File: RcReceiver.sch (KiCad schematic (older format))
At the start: 13 parts, among them U1 STM32L476VGT6, Y1 16MHz

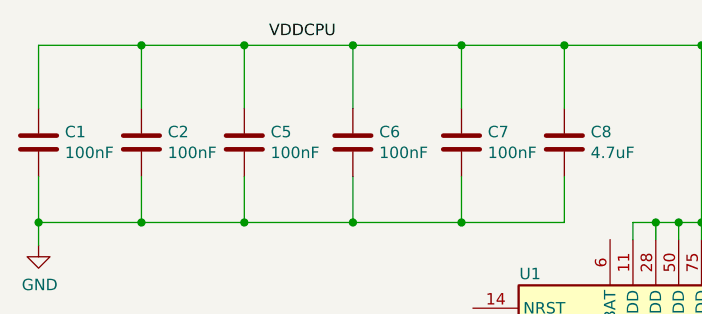
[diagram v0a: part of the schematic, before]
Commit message: Add footprints
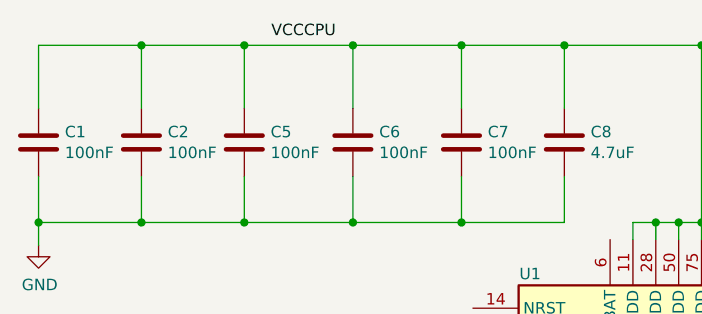
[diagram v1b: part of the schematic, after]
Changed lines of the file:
@@
 $EndComp
 Text Label 2025 900  2    50   ~ 0
-VDDCPU
+VCCCPU
 $Comp
 L Device:C C8

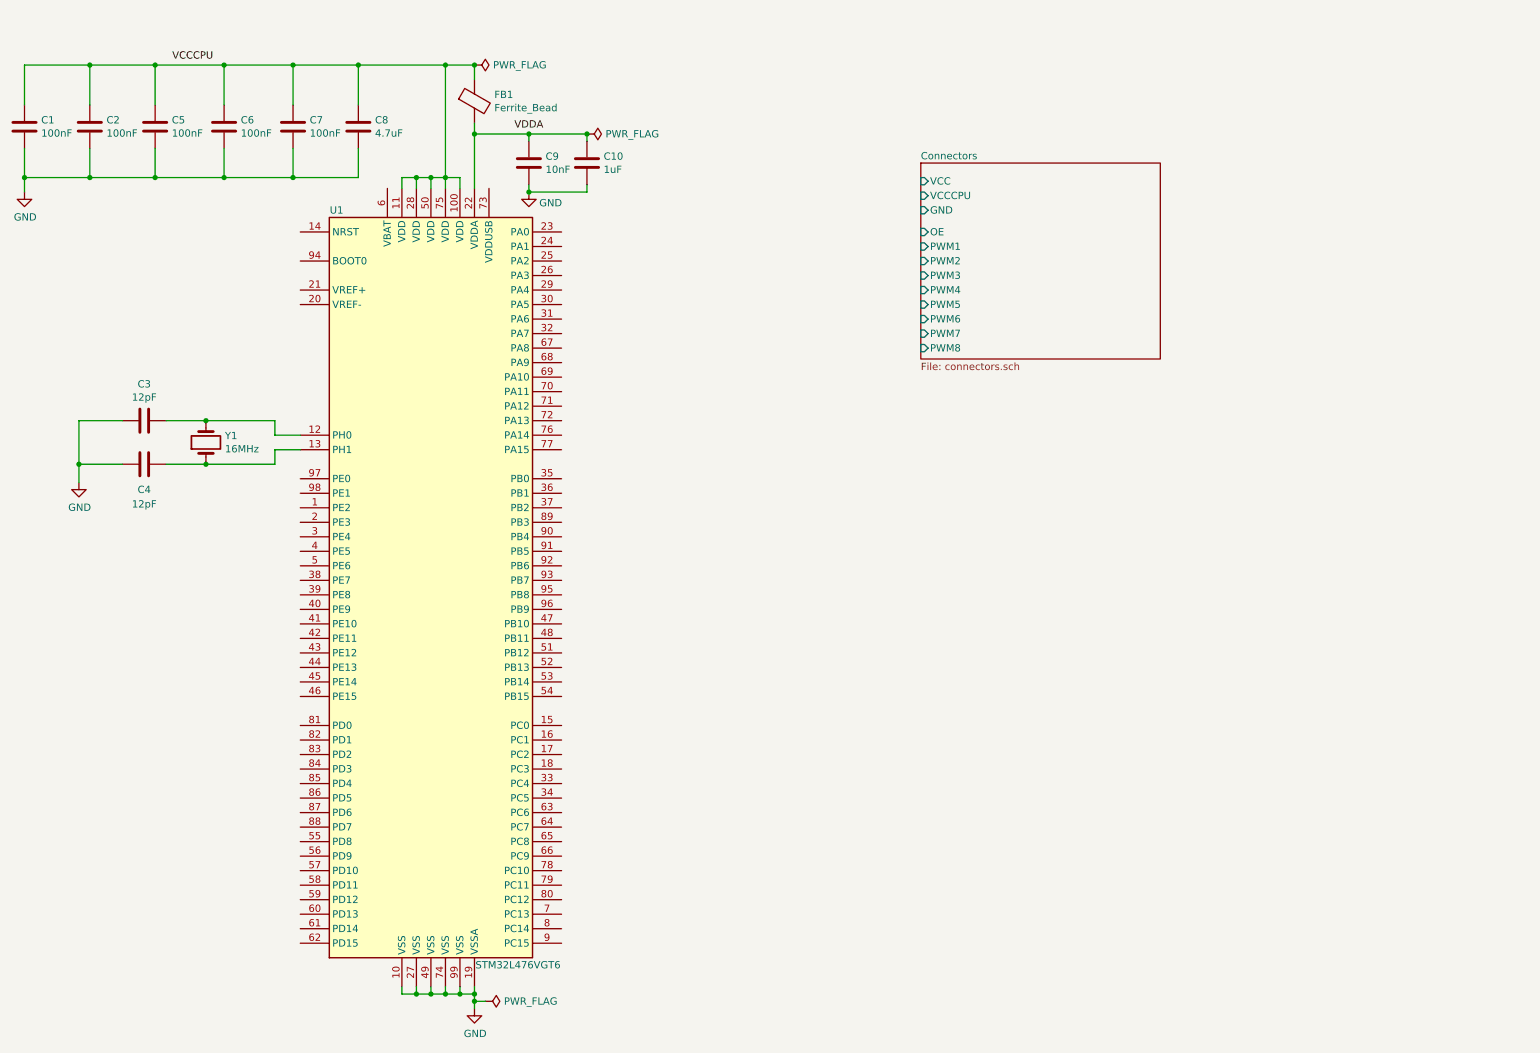
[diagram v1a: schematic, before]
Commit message: Add schema with RF modules
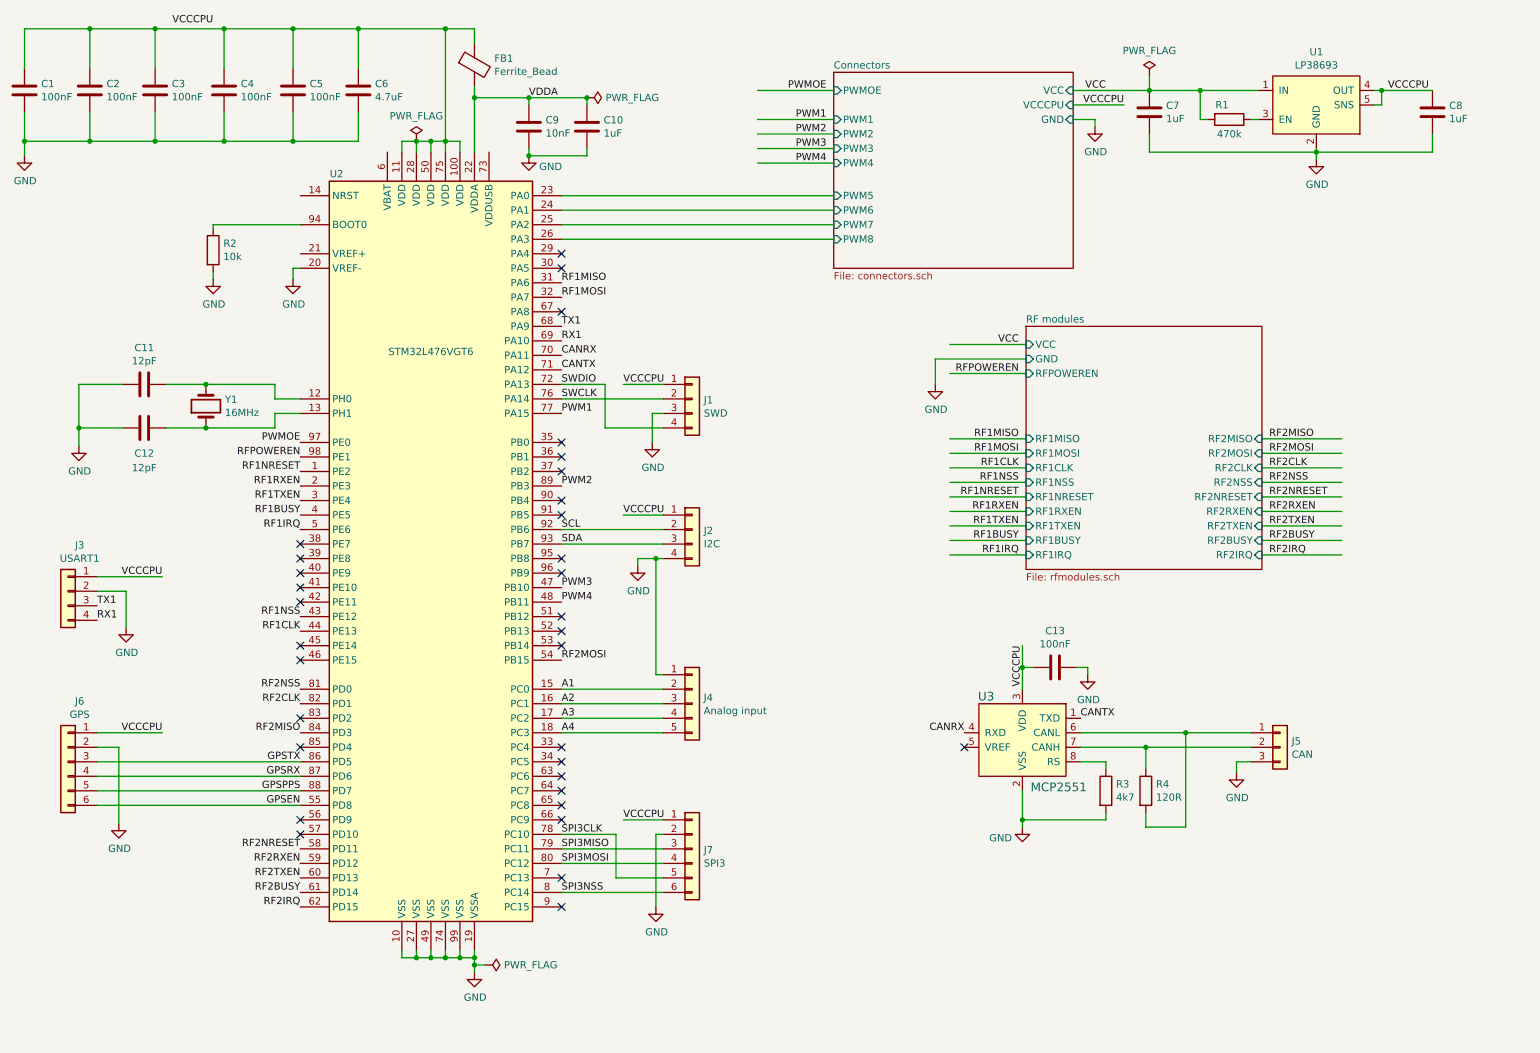
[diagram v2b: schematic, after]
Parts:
- added C13: 100nF, symbol Device:C
- added C7, C8: 1uF, symbol Device:C
- added J1: SWD, symbol Connector_Generic:Conn_01x04
- added J2: I2C, symbol Connector_Generic:Conn_01x04
- added J3: USART1, symbol Connector_Generic:Conn_01x04
- added J4: Analog input, symbol Connector_Generic:Conn_01x05
- added J5: CAN, symbol Connector_Generic:Conn_01x03
- added J6: GPS, symbol Connector_Generic:Conn_01x06
- added J7: SPI3, symbol Connector_Generic:Conn_01x06
- added R1: 470k, symbol Device:R
- added R2: 10k, symbol Device:R
- added R3: 4k7, symbol Device:R
- added R4: 120R, symbol Device:R
- added U1: LP38693, symbol LP38693:LP38693
- added U3: MCP2551, digikey-footprints:SOIC-8_W3.9mm, symbol dk_Interface-Drivers-Receivers-Transceivers:MCP2551-I_SN
- renumbered C3 to C11, C4 to C12, C5 to C3, C6 to C4, C7 to C5, C8 to C6, U1 to U2
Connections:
- net labels added: A1, A2, A3, A4, CANRX, CANTX, GPSEN, GPSPPS, GPSRX, GPSTX, PWM1, PWM2, PWM3, PWM4, PWMOE, RF1BUSY, RF1CLK, RF1IRQ, RF1MISO, RF1MOSI, RF1NRESET, RF1NSS, RF1RXEN, RF1TXEN, RF2BUSY, RF2CLK, RF2IRQ, RF2MISO, RF2MOSI, RF2NRESET, RF2NSS, RF2RXEN, RF2TXEN, RFPOWEREN, RX1, SCL, SDA, SPI3CLK, SPI3MISO, SPI3MOSI, SPI3NSS, SWCLK, SWDIO, TX1, VCC
- wire segments 71 -> 186
- no-connect marks 0 -> 33
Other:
- moved on the sheet: C1, C10, C11, C12, C2, C3, C4, C5, C6, C9, FB1, U2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

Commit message: Small changes
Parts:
- removed C13: 100nF, symbol Device:C
- removed J1: SWD, symbol Connector_Generic:Conn_01x04
- removed J5: CAN, symbol Connector_Generic:Conn_01x03
- removed R3: 4k7, symbol Device:R
- removed U3: MCP2551, digikey-footprints:SOIC-8_W3.9mm, symbol dk_Interface-Drivers-Receivers-Transceivers:MCP2551-I_SN
- added C11: 1uF, symbol Device:C
- added C12: 100nF, symbol Device:C
- added D1: LED, symbol Device:LED
- added D2: LED_ARGB, symbol Device:LED_ARGB
- added J1: VBAT, symbol Connector_Generic:Conn_01x02
- added J2: SWD, symbol Connector_Generic:Conn_01x05
- added R1: 2k2, symbol Device:R
- added R5, R6: 1k, symbol Device:R
- R4: value 120R -> 1k
- U1: value LP38693 -> LP38693-3.3
- renumbered C11 to C13, C12 to C14, J2 to J3, J3 to J4, J4 to J5, R1 to R2, R2 to R3
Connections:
- net labels added: LEDBLUE, LEDGREEN, LEDRED, NRST, VBAT
- wire segments 186 -> 190
- no-connect marks 33 -> 30
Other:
- moved on the sheet: J3, R3

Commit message: Final changes in schema
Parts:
- removed C11: 1uF, symbol Device:C
- removed C12: 100nF, symbol Device:C
- removed J3: I2C, symbol Connector_Generic:Conn_01x04
- removed J7: SPI3, symbol Connector_Generic:Conn_01x06
- added J3: I2C, symbol Connector_Generic:Conn_01x05
- added J7: SPI3, symbol Connector_Generic:Conn_01x07
- renumbered C13 to C11, C14 to C12
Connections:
- wire segments 190 -> 182
- no-connect marks 30 -> 29
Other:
- moved on the sheet: R3

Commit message: Add some footprints
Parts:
- removed Y1: 16MHz, symbol Device:Crystal
- added Y1: 16MHz, Oscillator:Oscillator_SMD_SeikoEpson_SG210-4Pin_2.5x2.0mm, symbol Device:Crystal_GND24
- C1, C10, C11, C12, C2, C3, C4, C5, C6, C7, C8, C9: footprint (none) -> Capacitor_SMD:C_0402_1005Metric
- D1: footprint (none) -> LED_SMD:LED_0402_1005Metric
- FB1: footprint (none) -> Inductor_SMD:L_0402_1005Metric
- J1: footprint (none) -> Connector_PinHeader_1.27mm:PinHeader_1x02_P1.27mm_Vertical
- J2, J3, J5: footprint (none) -> Connector_JST:JST_SH_BM05B-SRSS-TB_1x05-1MP_P1.00mm_Vertical
- J4: footprint (none) -> Connector_JST:JST_SH_BM04B-SRSS-TB_1x04-1MP_P1.00mm_Vertical
- J6: footprint (none) -> Connector_JST:JST_SH_BM06B-SRSS-TB_1x06-1MP_P1.00mm_Vertical
- J7: footprint (none) -> Connector_JST:JST_SH_BM07B-SRSS-TB_1x07-1MP_P1.00mm_Vertical
- R1, R2, R3, R4: footprint (none) -> Resistor_SMD:R_0402_1005Metric
- R5, R6: value 1k -> 470; footprint (none) -> Resistor_SMD:R_0402_1005Metric
- U1: footprint (none) -> miscellaneous:WSON-6_3x3mm_Pitch0.95mm
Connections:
- wire segments 182 -> 188
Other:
- moved on the sheet: C11, C12
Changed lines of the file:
@@
 EESchema Schematic File Version 4
+LIBS:RcReceiver-cache
 EELAYER 26 0
 EELAYER END
@@
 $EndDescr
 $Comp
-L Device:Crystal Y1
-U 1 1 5C749939
-P 1975 3275
-F 0 "Y1" V 2021 3144 50  0000 R CNN
-F 1 "16MHz" V 1930 3144 50  0000 R CNN
-F 2 "" H 1975 3275 50  0001 C CNN
-F 3 "~" H 1975 3275 50  0001 C CNN
-	1    1975 3275
-	0    -1   -1   0
-$EndComp
-$Comp
 L Device:C C12
 U 1 1 5C749996
-P 1550 3425
-F 0 "C12" V 1725 3425 50  0000 C CNN
-F 1 "12pF" V 1825 3425 50  0000 C CNN
-F 2 "" H 1588 3275 50  0001 C CNN
-F 3 "~" H 1550 3425 50  0001 C CNN
-	1    1550 3425
+P 1375 3450
+F 0 "C12" V 1550 3450 50  0000 C CNN
+F 1 "12pF" V 1650 3450 50  0000 C CNN
+F 2 "Capacitor_SMD:C_0402_1005Metric" H 1413 3300 50  0001 C CNN
+F 3 "~" H 1375 3450 50  0001 C CNN
+	1    1375 3450
 	0    1    1    0
 $EndComp
@@
 L Device:C C11
 U 1 1 5C7499E6
-P 1550 3125
-F 0 "C11" V 1298 3125 50  0000 C CNN
-F 1 "12pF" V 1389 3125 50  0000 C CNN
-F 2 "" H 1588 2975 50  0001 C CNN
-F 3 "~" H 1550 3125 50  0001 C CNN
-	1    1550 3125
+P 1375 3100
+F 0 "C11" V 1123 3100 50  0000 C CNN
+F 1 "12pF" V 1214 3100 50  0000 C CNN
+F 2 "Capacitor_SMD:C_0402_1005Metric" H 1413 2950 50  0001 C CNN
+F 3 "~" H 1375 3100 50  0001 C CNN
+	1    1375 3100
 	0    1    1    0
 $EndComp
 Wire Wire Line
-	1700 3425 1975 3425
-Wire Wire Line
-	1975 3425 2450 3425
-Wire Wire Line
-	2450 3425 2450 3325
+	2450 3450 2450 3325
 Wire Wire Line
 	2450 3325 2625 3325
-Connection ~ 1975 3425
-Wire Wire Line
-	1700 3125 1975 3125
-Wire Wire Line
-	1975 3125 2450 3125
-Wire Wire Line
-	2450 3125 2450 3225
 Wire Wire Line
 	2450 3225 2625 3225
-Connection ~ 1975 3125
 $Comp
 L power:GND #PWR010
@@
 $EndComp
 Wire Wire Line
-	1100 3550 1100 3425
-Wire Wire Line
-	1100 3125 1400 3125
-Wire Wire Line
-	1400 3425 1100 3425
-Connection ~ 1100 3425
-Wire Wire Line
-	1100 3425 1100 3125
+	1100 3550 1100 3450
+Wire Wire Line
+	1100 3100 1225 3100
+Wire Wire Line
+	1225 3450 1100 3450
+Connection ~ 1100 3450
+Wire Wire Line
+	1100 3450 1100 3100
 $Comp
 L power:PWR_FLAG #FLG04
@@
 F 0 "C1" H 840 1146 50  0000 L CNN
 F 1 "100nF" H 840 1055 50  0000 L CNN
-F 2 "" H 763 950 50  0001 C CNN
+F 2 "Capacitor_SMD:C_0402_1005Metric" H 763 950 50  0001 C CNN
 F 3 "~" H 725 1100 50  0001 C CNN
 	1    725  1100
@@
 F 0 "C2" H 1290 1146 50  0000 L CNN
 F 1 "100nF" H 1290 1055 50  0000 L CNN
-F 2 "" H 1213 950 50  0001 C CNN
+F 2 "Capacitor_SMD:C_0402_1005Metric" H 1213 950 50  0001 C CNN
 F 3 "~" H 1175 1100 50  0001 C CNN
 	1    1175 1100
@@
 F 0 "C3" H 1740 1146 50  0000 L CNN
 F 1 "100nF" H 1740 1055 50  0000 L CNN
-F 2 "" H 1663 950 50  0001 C CNN
+F 2 "Capacitor_SMD:C_0402_1005Metric" H 1663 950 50  0001 C CNN
 F 3 "~" H 1625 1100 50  0001 C CNN
 	1    1625 1100
@@
 F 0 "C4" H 2215 1146 50  0000 L CNN
 F 1 "100nF" H 2215 1055 50  0000 L CNN
-F 2 "" H 2138 950 50  0001 C CNN
+F 2 "Capacitor_SMD:C_0402_1005Metric" H 2138 950 50  0001 C CNN
 F 3 "~" H 2100 1100 50  0001 C CNN
 	1    2100 1100
@@
 F 0 "C5" H 2690 1146 50  0000 L CNN
 F 1 "100nF" H 2690 1055 50  0000 L CNN
-F 2 "" H 2613 950 50  0001 C CNN
+F 2 "Capacitor_SMD:C_0402_1005Metric" H 2613 950 50  0001 C CNN
 F 3 "~" H 2575 1100 50  0001 C CNN
 	1    2575 1100
@@
 F 0 "C6" H 3140 1146 50  0000 L CNN
 F 1 "4.7uF" H 3140 1055 50  0000 L CNN
-F 2 "" H 3063 950 50  0001 C CNN
+F 2 "Capacitor_SMD:C_0402_1005Metric" H 3063 950 50  0001 C CNN
 F 3 "~" H 3025 1100 50  0001 C CNN
 	1    3025 1100
@@
 F 0 "C9" H 4315 1396 50  0000 L CNN
 F 1 "10nF" H 4315 1305 50  0000 L CNN
-F 2 "" H 4238 1200 50  0001 C CNN
+F 2 "Capacitor_SMD:C_0402_1005Metric" H 4238 1200 50  0001 C CNN
 F 3 "~" H 4200 1350 50  0001 C CNN
 	1    4200 1350
@@
 F 0 "C10" H 4715 1396 50  0000 L CNN
 F 1 "1uF" H 4715 1305 50  0000 L CNN
-F 2 "" H 4638 1200 50  0001 C CNN
+F 2 "Capacitor_SMD:C_0402_1005Metric" H 4638 1200 50  0001 C CNN
 F 3 "~" H 4600 1350 50  0001 C CNN
 	1    4600 1350
@@
 F 0 "FB1" H 3962 971 50  0000 L CNN
 F 1 "Ferrite_Bead" H 3962 880 50  0000 L CNN
-F 2 "" V 3755 925 50  0001 C CNN
+F 2 "Inductor_SMD:L_0402_1005Metric" V 3755 925 50  0001 C CNN
 F 3 "~" H 3825 925 50  0001 C CNN
 	1    3825 925
@@
 F 0 "R3" H 2120 2221 50  0000 L CNN
 F 1 "10k" H 2120 2130 50  0000 L CNN
-F 2 "" V 1980 2175 50  0001 C CNN
+F 2 "Resistor_SMD:R_0402_1005Metric" V 1980 2175 50  0001 C CNN
 F 3 "~" H 2050 2175 50  0001 C CNN
 	1    2050 2175
@@
 F 0 "U1" H 9625 1565 50  0000 C CNN
 F 1 "LP38693-3.3" H 9625 1474 50  0000 C CNN
-F 2 "" H 9625 1200 50  0001 C CNN
+F 2 "miscellaneous:WSON-6_3x3mm_Pitch0.95mm" H 9625 1200 50  0001 C CNN
 F 3 "http://www.ti.com/lit/ds/snvs321o/snvs321o.pdf" H 9625 1200 50  0001 C CNN
 	1    9625 1200
@@
 F 0 "C8" H 10540 1296 50  0000 L CNN
 F 1 "1uF" H 10540 1205 50  0000 L CNN
-F 2 "" H 10463 1100 50  0001 C CNN
+F 2 "Capacitor_SMD:C_0402_1005Metric" H 10463 1100 50  0001 C CNN
 F 3 "~" H 10425 1250 50  0001 C CNN
 	1    10425 1250
@@
 F 0 "C7" H 8590 1296 50  0000 L CNN
 F 1 "1uF" H 8590 1205 50  0000 L CNN
-F 2 "" H 8513 1100 50  0001 C CNN
+F 2 "Capacitor_SMD:C_0402_1005Metric" H 8513 1100 50  0001 C CNN
 F 3 "~" H 8475 1250 50  0001 C CNN
 	1    8475 1250
@@
 F 0 "R2" V 8925 1250 50  0000 C CNN
 F 1 "470k" V 9125 1300 50  0000 C CNN
-F 2 "" V 8955 1300 50  0001 C CNN
+F 2 "Resistor_SMD:R_0402_1005Metric" V 8955 1300 50  0001 C CNN
 F 3 "~" H 9025 1300 50  0001 C CNN
 	1    9025 1300
@@
 F 0 "J5" H 5404 5367 50  0000 L CNN
 F 1 "Analog input" H 5404 5276 50  0000 L CNN
-F 2 "" H 5325 5325 50  0001 C CNN
+F 2 "Connector_JST:JST_SH_BM05B-SRSS-TB_1x05-1MP_P1.00mm_Vertical" H 5325 5325 50  0001 C CNN
 F 3 "~" H 5325 5325 50  0001 C CNN
 	1    5325 5325
@@
 F 0 "J6" H 945 6142 50  0000 C CNN
 F 1 "GPS" H 945 6051 50  0000 C CNN
-F 2 "" H 1025 5725 50  0001 C CNN
+F 2 "Connector_JST:JST_SH_BM06B-SRSS-TB_1x06-1MP_P1.00mm_Vertical" H 1025 5725 50  0001 C CNN
 F 3 "~" H 1025 5725 50  0001 C CNN
 	1    1025 5725
@@
 F 0 "J4" H 945 4867 50  0000 C CNN
 F 1 "USART1" H 945 4776 50  0000 C CNN
-F 2 "" H 1025 4550 50  0001 C CNN
+F 2 "Connector_JST:JST_SH_BM04B-SRSS-TB_1x04-1MP_P1.00mm_Vertical" H 1025 4550 50  0001 C CNN
 F 3 "~" H 1025 4550 50  0001 C CNN
 	1    1025 4550
@@
 F 0 "J2" H 5405 3367 50  0000 L CNN
 F 1 "SWD" H 5405 3276 50  0000 L CNN
-F 2 "" H 5325 3325 50  0001 C CNN
+F 2 "Connector_JST:JST_SH_BM05B-SRSS-TB_1x05-1MP_P1.00mm_Vertical" H 5325 3325 50  0001 C CNN
 F 3 "~" H 5325 3325 50  0001 C CNN
 	1    5325 3325
@@
 F 0 "R1" H 10870 1321 50  0000 L CNN
 F 1 "2k2" H 10870 1230 50  0000 L CNN
-F 2 "" V 10730 1275 50  0001 C CNN
+F 2 "Resistor_SMD:R_0402_1005Metric" V 10730 1275 50  0001 C CNN
 F 3 "~" H 10800 1275 50  0001 C CNN
 	1    10800 1275
@@
 F 0 "D1" V 10838 1633 50  0000 R CNN
 F 1 "LED" V 10747 1633 50  0000 R CNN
-F 2 "" H 10800 1750 50  0001 C CNN
+F 2 "LED_SMD:LED_0402_1005Metric" H 10800 1750 50  0001 C CNN
 F 3 "~" H 10800 1750 50  0001 C CNN
 	1    10800 1750
@@
 F 0 "R4" V 1750 6975 50  0000 C CNN
 F 1 "1k" V 1825 6975 50  0000 C CNN
-F 2 "" V 1755 6975 50  0001 C CNN
+F 2 "Resistor_SMD:R_0402_1005Metric" V 1755 6975 50  0001 C CNN
 F 3 "~" H 1825 6975 50  0001 C CNN
 	1    1825 6975
@@
 P 1825 7175
 F 0 "R5" V 1750 7175 50  0000 C CNN
-F 1 "1k" V 1825 7175 50  0000 C CNN
-F 2 "" V 1755 7175 50  0001 C CNN
+F 1 "470" V 1825 7175 50  0000 C CNN
+F 2 "Resistor_SMD:R_0402_1005Metric" V 1755 7175 50  0001 C CNN
 F 3 "~" H 1825 7175 50  0001 C CNN
 	1    1825 7175
@@
 P 1825 7375
 F 0 "R6" V 1750 7375 50  0000 C CNN
-F 1 "1k" V 1825 7375 50  0000 C CNN
-F 2 "" V 1755 7375 50  0001 C CNN
+F 1 "470" V 1825 7375 50  0000 C CNN
+F 2 "Resistor_SMD:R_0402_1005Metric" V 1755 7375 50  0001 C CNN
 F 3 "~" H 1825 7375 50  0001 C CNN
 	1    1825 7375
@@
 F 0 "J1" H 5404 2442 50  0000 L CNN
 F 1 "VBAT" H 5404 2351 50  0000 L CNN
-F 2 "" H 5325 2450 50  0001 C CNN
+F 2 "Connector_PinHeader_1.27mm:PinHeader_1x02_P1.27mm_Vertical" H 5325 2450 50  0001 C CNN
 F 3 "~" H 5325 2450 50  0001 C CNN
 	1    5325 2450
@@
 F 0 "J3" H 5405 4167 50  0000 L CNN
 F 1 "I2C" H 5405 4076 50  0000 L CNN
-F 2 "" H 5325 4125 50  0001 C CNN
+F 2 "Connector_JST:JST_SH_BM05B-SRSS-TB_1x05-1MP_P1.00mm_Vertical" H 5325 4125 50  0001 C CNN
 F 3 "~" H 5325 4125 50  0001 C CNN
 	1    5325 4125
@@
 F 0 "J7" H 5405 6467 50  0000 L CNN
 F 1 "SPI3" H 5405 6376 50  0000 L CNN
-F 2 "" H 5325 6425 50  0001 C CNN
+F 2 "Connector_JST:JST_SH_BM07B-SRSS-TB_1x07-1MP_P1.00mm_Vertical" H 5325 6425 50  0001 C CNN
 F 3 "~" H 5325 6425 50  0001 C CNN
 	1    5325 6425
@@
 Wire Wire Line
 	4425 6725 5125 6725
+$Comp
+L power:GND #PWR0101
+U 1 1 5CE8974D
+P 1625 3550
+F 0 "#PWR0101" H 1625 3300 50  0001 C CNN
+F 1 "GND" H 1630 3377 50  0000 C CNN
+F 2 "" H 1625 3550 50  0001 C CNN
+F 3 "" H 1625 3550 50  0001 C CNN
+	1    1625 3550
+	1    0    0    -1
+$EndComp
+$Comp
+L power:GND #PWR0102
+U 1 1 5CE8980F
+P 2075 3550
+F 0 "#PWR0102" H 2075 3300 50  0001 C CNN
+F 1 "GND" H 2080 3377 50  0000 C CNN
+F 2 "" H 2075 3550 50  0001 C CNN
+F 3 "" H 2075 3550 50  0001 C CNN
+	1    2075 3550
+	1    0    0    -1
+$EndComp
+Wire Wire Line
+	1625 3550 1625 3275
+Wire Wire Line
+	1625 3275 1650 3275
+Wire Wire Line
+	2075 3550 2075 3275
+Wire Wire Line
+	2075 3275 2050 3275
+$Comp
+L Device:Crystal_GND24 Y1
+U 1 1 5CE6BFA7
+P 1850 3275
+F 0 "Y1" V 1775 3525 50  0000 L CNN
+F 1 "16MHz" V 1875 3525 50  0000 L CNN
+F 2 "Oscillator:Oscillator_SMD_SeikoEpson_SG210-4Pin_2.5x2.0mm" H 1850 3275 50  0001 C CNN
+F 3 "~" H 1850 3275 50  0001 C CNN
+	1    1850 3275
+	0    1    1    0
+$EndComp
+Wire Wire Line
+	1525 3100 1850 3100
+Wire Wire Line
+	2450 3100 2450 3225
+Wire Wire Line
+	1525 3450 1850 3450
+Wire Wire Line
+	1850 3100 1850 3125
+Connection ~ 1850 3100
+Wire Wire Line
+	1850 3100 2450 3100
+Wire Wire Line
+	1850 3450 1850 3425
+Connection ~ 1850 3450
+Wire Wire Line
+	1850 3450 2450 3450
 $EndSCHEMATC

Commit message: Create PCB
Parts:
- D2: footprint (none) -> miscellaneous:LED_Lumex-LX0404
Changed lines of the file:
@@
 F 0 "D2" H 1400 7672 50  0000 C CNN
 F 1 "LED_ARGB" H 1400 7581 50  0000 C CNN
-F 2 "" H 1400 7125 50  0001 C CNN
+F 2 "miscellaneous:LED_Lumex-LX0404" H 1400 7125 50  0001 C CNN
 F 3 "~" H 1400 7125 50  0001 C CNN
 	1    1400 7175

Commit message: Place all the components on the board
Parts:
- added C33: 100nF, Capacitor_SMD:C_0402_1005Metric, symbol Device:C
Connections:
- wire segments 188 -> 193
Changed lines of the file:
@@
 $EndComp
 Wire Wire Line
-	2050 2375 2050 2325
+	2050 2375 2050 2350
 $Sheet
 S 7550 3775 1625 1675
@@
 Wire Wire Line
 	1850 3450 2450 3450
+$Comp
+L Device:C C33
+U 1 1 5CF3CB0A
+P 1650 2150
+F 0 "C33" H 1765 2196 50  0000 L CNN
+F 1 "100nF" H 1765 2105 50  0000 L CNN
+F 2 "Capacitor_SMD:C_0402_1005Metric" H 1688 2000 50  0001 C CNN
+F 3 "~" H 1650 2150 50  0001 C CNN
+	1    1650 2150
+	1    0    0    -1
+$EndComp
+Wire Wire Line
+	2050 2350 1650 2350
+Wire Wire Line
+	1650 2350 1650 2300
+Connection ~ 2050 2350
+Wire Wire Line
+	2050 2350 2050 2325
+Wire Wire Line
+	1650 2000 1650 1825
+Wire Wire Line
+	1650 1825 2625 1825
 $EndSCHEMATC
